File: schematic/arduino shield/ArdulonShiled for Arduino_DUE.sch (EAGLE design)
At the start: 25 parts, among them X1 5566-14, X2 5566-14, X3 5566-14

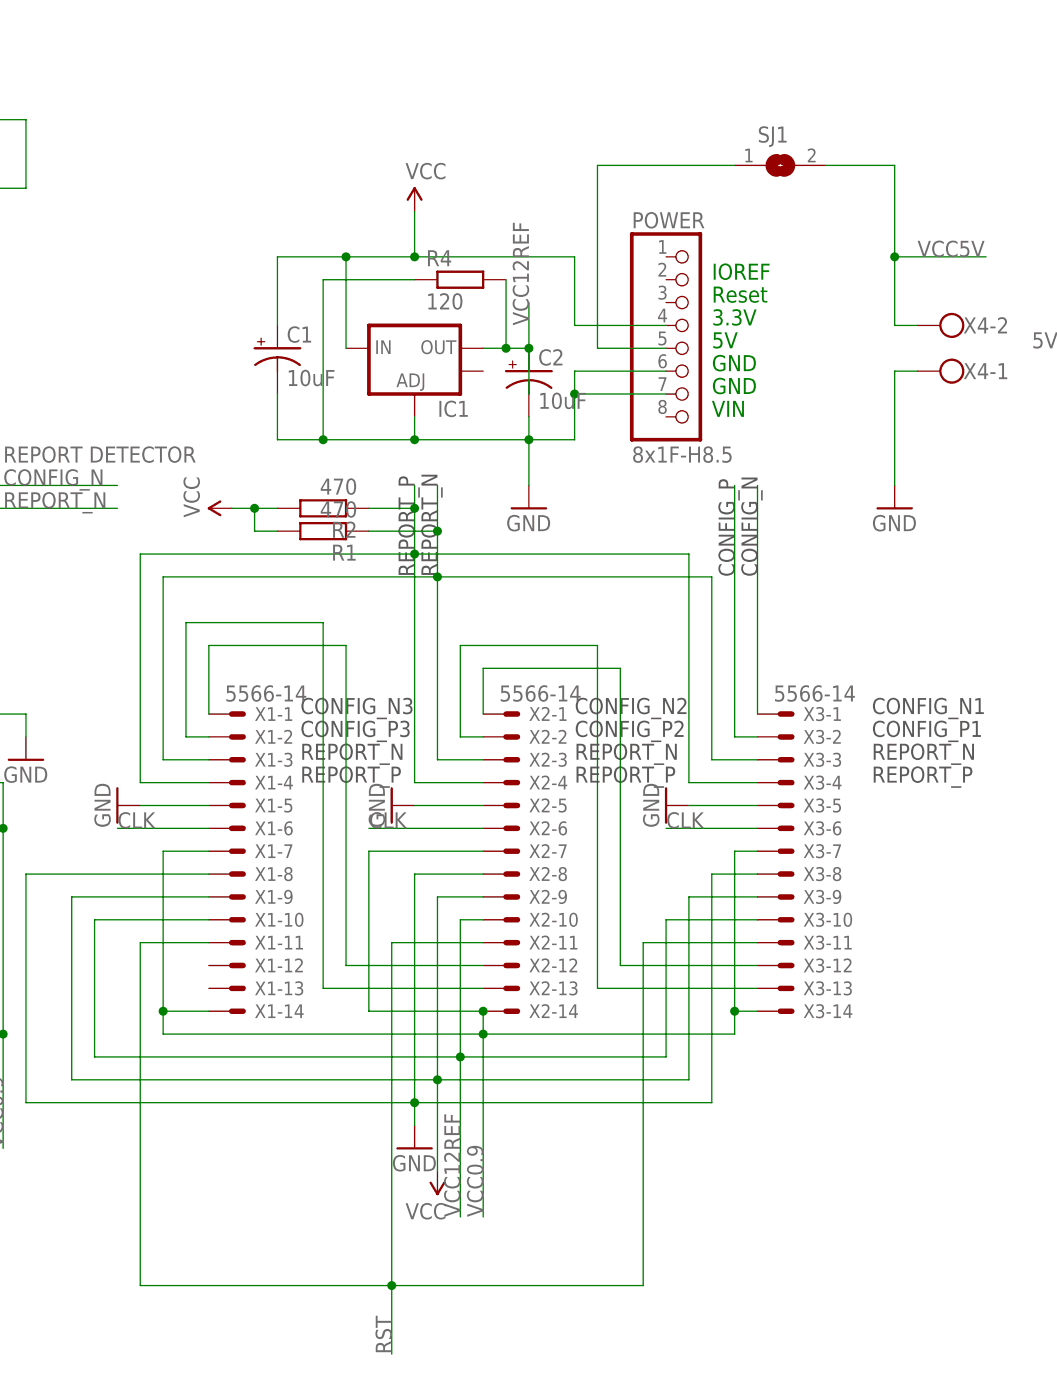
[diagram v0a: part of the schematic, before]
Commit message: added some datasheets, updated schematic
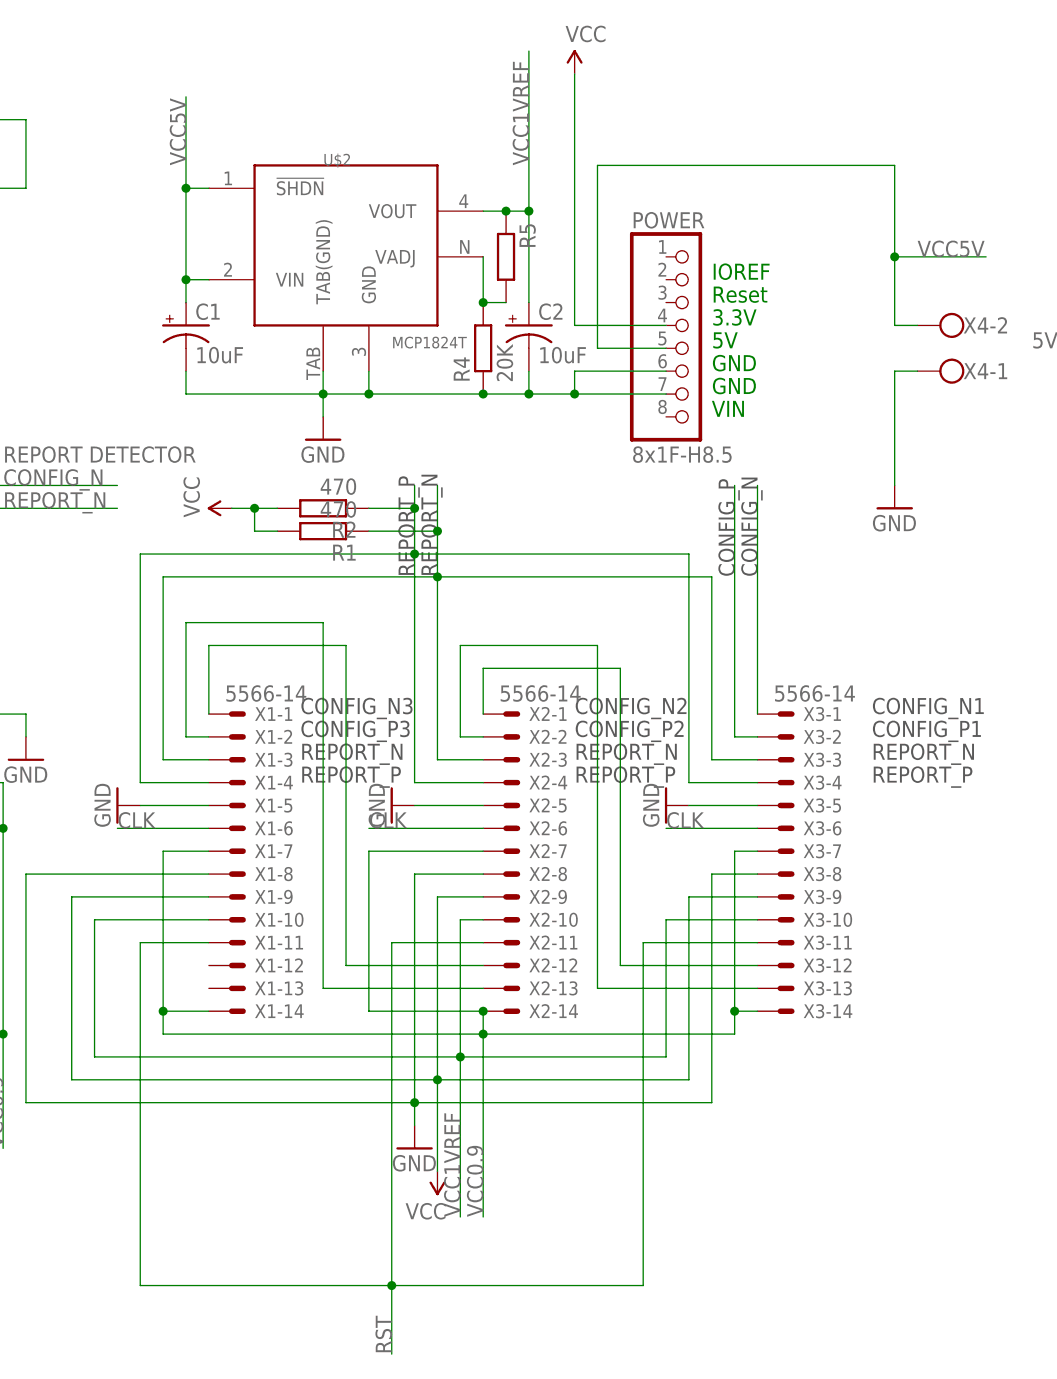
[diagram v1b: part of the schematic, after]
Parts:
- removed IC1: (no value), SparkFun:V_REG_LM1117SOT223
- removed SJ1: (no value), jumper:SJ
- added R5: (no value), rcl:R-EU_M0805
- added U$2: MCP1824T, BaseApp:MCP1824T
- R4: value 120 -> 20K
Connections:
- net VCC12 renamed VCC0.9
- removed net VCC12REF: C2.+, IC1.OUT, R4.2, X1-10.S, X2-10.S, X3-10.S
- new net VCC1REF: C2.+, R5.1, U$2.VOUT, X1-10.S, X2-10.S, X3-10.S
- net GND: now also U$2.GND, U$2.TAB(GND); no longer IC1.ADJ
- net N$1: now also R4.2, R5.2, U$2.VADJ; no longer POWER.5, SJ1.1
- net VCC: no longer C1.+, IC1.IN
- net VCC5V: now also C1.+, POWER.5, U$2.!SHDN, U$2.VIN; no longer SJ1.2
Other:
- note added: "VCC1VREF"
- note removed: "VCC12REF"
- moved on the sheet: C1, C2, R4
